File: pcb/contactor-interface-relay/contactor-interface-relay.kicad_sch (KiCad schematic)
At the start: 11 parts, among them J1 Conn_01x04_Socket, K1 G5LE-1

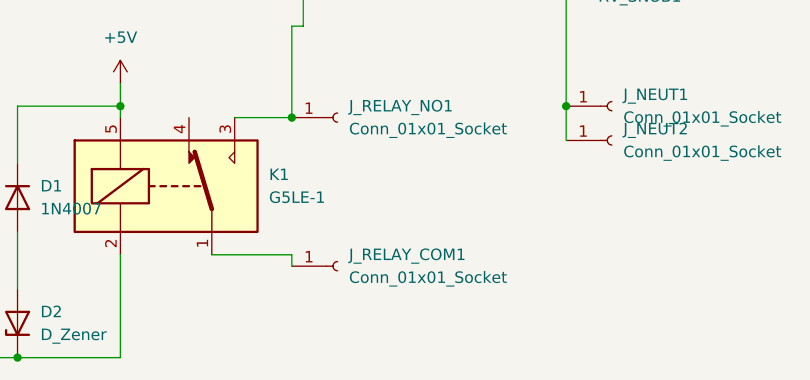
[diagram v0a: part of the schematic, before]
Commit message: Adding fuse for contactor coil
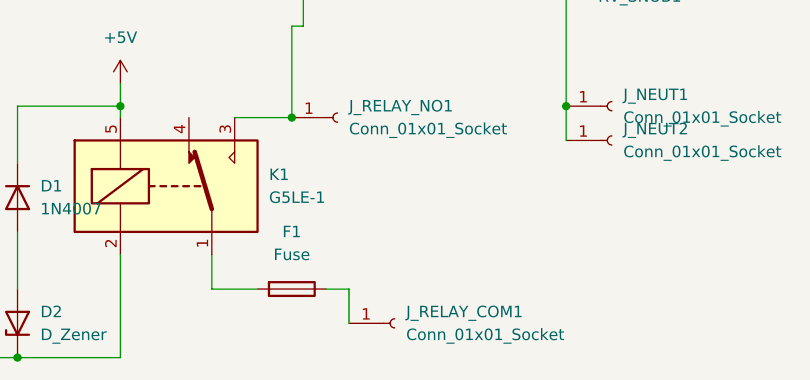
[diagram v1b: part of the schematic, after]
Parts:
- added F1: Fuse, Fuse:Fuse_Littelfuse_395Series, symbol Device:Fuse
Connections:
- net at J_RELAY_COM1.1 (Pin_1): now also F1.1; no longer K1.1
- new net: F1.2, K1.1
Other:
- moved on the sheet: J_RELAY_COM1
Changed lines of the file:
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@@
-	(wire
-		(pts
-			(xy 109.22 78.74) (xy 118.11 78.74)
-		)
-		(stroke
-			(width 0)
-			(type default)
-		)
-	)
 	(wire
 		(pts
@@
 	(wire
 		(pts
+			(xy 109.22 82.55) (xy 109.22 78.74)
+		)
+		(stroke
+			(width 0)
+			(type default)
+		)
+	)
+	(wire
+		(pts
 			(xy 99.06 62.23) (xy 99.06 63.5)
 		)
@@
 	(wire
 		(pts
+			(xy 121.92 82.55) (xy 124.46 82.55)
+		)
+		(stroke
+			(width 0)
+			(type default)
+		)
+	)
+	(wire
+		(pts
 			(xy 78.74 90.17) (xy 87.63 90.17)
 		)
@@
 	(wire
 		(pts
+			(xy 109.22 82.55) (xy 114.3 82.55)
+		)
+		(stroke
+			(width 0)
+			(type default)
+		)
+	)
+	(wire
+		(pts
 			(xy 111.76 63.5) (xy 118.11 63.5)
 		)
@@
 	(wire
 		(pts
-			(xy 118.11 78.74) (xy 118.11 80.01)
+			(xy 124.46 82.55) (xy 124.46 86.36)
 		)
 		(stroke
@@
 	)
 	(symbol
+		(lib_id "Device:Fuse")
+		(at 118.11 82.55 270)
+		(unit 1)
+		(exclude_from_sim no)
+		(in_bom yes)
+		(on_board yes)
+		(dnp no)
+		(fields_autoplaced yes)
+		(property "Reference" "F1"
+			(at 118.11 76.2 90)
+			(effects
+				(font
+					(size 1.27 1.27)
+				)
+			)
+		)
+		(property "Value" "Fuse"
+			(at 118.11 78.74 90)
+			(effects
+				(font
+					(size 1.27 1.27)
+				)
+			)
+		)
+		(property "Footprint" "Fuse:Fuse_Littelfuse_395Series"
+			(at 118.11 80.772 90)
+			(effects
+				(font
+					(size 1.27 1.27)
+				)
+				(hide yes)
+			)
+		)
+		(property "Datasheet" "~"
+			(at 118.11 82.55 0)
+			(effects
+				(font
+					(size 1.27 1.27)
+				)
+				(hide yes)
+			)
+		)
+		(property "Description" "Fuse"
+			(at 118.11 82.55 0)
+			(effects
+				(font
+					(size 1.27 1.27)
+				)
+				(hide yes)
+			)
+		)
+		(pin "1"
+		)
+		(pin "2"
+		)
+		(instances
+			(project ""
+				(path "/92cf2299-4756-44c6-9b64-4b60cc6635f5"
+					(reference "F1")
+					(unit 1)
+				)
+			)
+		)
+	)
+	(symbol
 		(lib_id "power:NEUT")
 		(at 124.46 48.26 0)
@@
 	(symbol
 		(lib_id "Connector:Conn_01x01_Socket")
-		(at 123.19 80.01 0)
+		(at 129.54 86.36 0)
 		(unit 1)
 		(exclude_from_sim no)
@@
 		(fields_autoplaced yes)
 		(property "Reference" "J_RELAY_COM1"
-			(at 124.46 78.7399 0)
+			(at 130.81 85.0899 0)
 			(effects
 				(font
@@
 		)
 		(property "Value" "Conn_01x01_Socket"
-			(at 124.46 81.2799 0)
+			(at 130.81 87.6299 0)
 			(effects
 				(font
@@
 		)
 		(property "Footprint" "Connector_Wire:SolderWire-2.5sqmm_1x01_D2.4mm_OD4.4mm"
-			(at 123.19 80.01 0)
+			(at 129.54 86.36 0)
 			(effects
 				(font
@@
 		)
 		(property "Datasheet" "~"
-			(at 123.19 80.01 0)
+			(at 129.54 86.36 0)
 			(effects
 				(font
@@
 		)
 		(property "Description" "Generic connector, single row, 01x01, script generated"
-			(at 123.19 80.01 0)
-			(effects
-				(font
+			(at 129.54 86.36 0)
+			(effects
+				(font

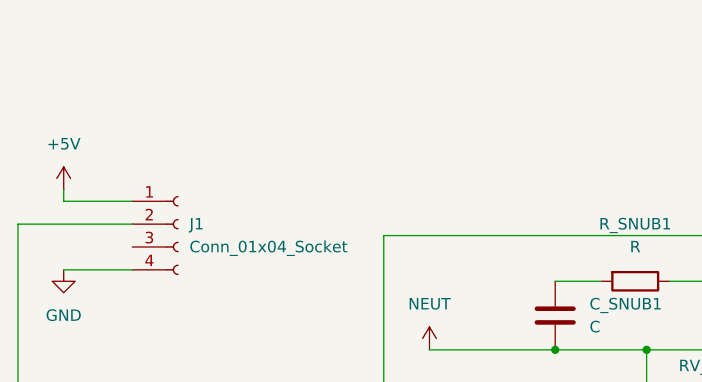
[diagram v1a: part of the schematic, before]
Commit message: Extra 5v / ground connections
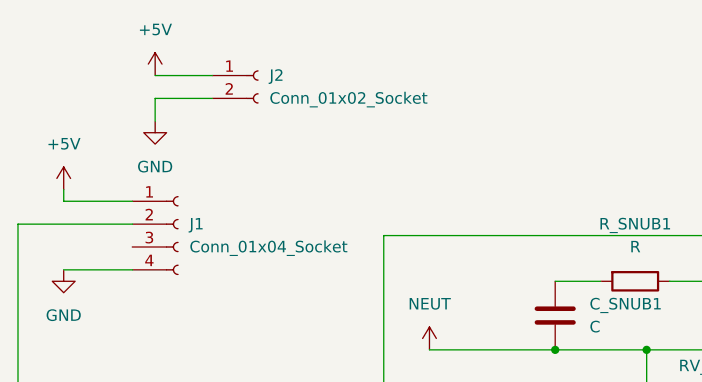
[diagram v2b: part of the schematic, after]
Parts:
- added J2: Conn_01x02_Socket, Connector_PinHeader_2.54mm:PinHeader_1x02_P2.54mm_Vertical, symbol Connector:Conn_01x02_Socket
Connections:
- net +5V: now also J2.1 (Pin_1)
- net GND: now also J2.2 (Pin_2)
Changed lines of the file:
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@@
+	(wire
+		(pts
+			(xy 93.98 17.78) (xy 100.33 17.78)
+		)
+		(stroke
+			(width 0)
+			(type default)
+		)
+	)
 	(wire
 		(pts
@@
 	(wire
 		(pts
+			(xy 93.98 20.32) (xy 93.98 22.86)
+		)
+		(stroke
+			(width 0)
+			(type default)
+		)
+	)
+	(wire
+		(pts
 			(xy 83.82 39.37) (xy 91.44 39.37)
 		)
@@
 	(wire
 		(pts
+			(xy 100.33 20.32) (xy 93.98 20.32)
+		)
+		(stroke
+			(width 0)
+			(type default)
+		)
+	)
+	(wire
+		(pts
 			(xy 91.44 31.75) (xy 83.82 31.75)
 		)
@@
 			(width 0)
 			(type default)
+		)
+	)
+	(symbol
+		(lib_id "Connector:Conn_01x02_Socket")
+		(at 105.41 17.78 0)
+		(unit 1)
+		(exclude_from_sim no)
+		(in_bom yes)
+		(on_board yes)
+		(dnp no)
+		(fields_autoplaced yes)
+		(property "Reference" "J2"
+			(at 106.68 17.7799 0)
+			(effects
+				(font
+					(size 1.27 1.27)
+				)
+				(justify left)
+			)
+		)
+		(property "Value" "Conn_01x02_Socket"
+			(at 106.68 20.3199 0)
+			(effects
+				(font
+					(size 1.27 1.27)
+				)
+				(justify left)
+			)
+		)
+		(property "Footprint" "Connector_PinHeader_2.54mm:PinHeader_1x02_P2.54mm_Vertical"
+			(at 105.41 17.78 0)
+			(effects
+				(font
+					(size 1.27 1.27)
+				)
+				(hide yes)
+			)
+		)
+		(property "Datasheet" "~"
+			(at 105.41 17.78 0)
+			(effects
+				(font
+					(size 1.27 1.27)
+				)
+				(hide yes)
+			)
+		)
+		(property "Description" "Generic connector, single row, 01x02, script generated"
+			(at 105.41 17.78 0)
+			(effects
+				(font
+					(size 1.27 1.27)
+				)
+				(hide yes)
+			)
+		)
+		(pin "1"
+		)
+		(pin "2"
+		)
+		(instances
+			(project ""
+				(path "/92cf2299-4756-44c6-9b64-4b60cc6635f5"
+					(reference "J2")
+					(unit 1)
+				)
+			)
 		)
 	)
@@
 	)
 	(symbol
+		(lib_id "power:GND")
+		(at 93.98 22.86 0)
+		(unit 1)
+		(exclude_from_sim no)
+		(in_bom yes)
+		(on_board yes)
+		(dnp no)
+		(fields_autoplaced yes)
+		(property "Reference" "#PWR6"
+			(at 93.98 29.21 0)
+			(effects
+				(font
+					(size 1.27 1.27)
+				)
+				(hide yes)
+			)
+		)
+		(property "Value" "GND"
+			(at 93.98 27.94 0)
+			(effects
+				(font
+					(size 1.27 1.27)
+				)
+			)
+		)
+		(property "Footprint" ""
+			(at 93.98 22.86 0)
+			(effects
+				(font
+					(size 1.27 1.27)
+				)
+				(hide yes)
+			)
+		)
+		(property "Datasheet" ""
+			(at 93.98 22.86 0)
+			(effects
+				(font
+					(size 1.27 1.27)
+				)
+				(hide yes)
+			)
+		)
+		(property "Description" "Power symbol creates a global label with name \"GND\" , ground"
+			(at 93.98 22.86 0)
+			(effects
+				(font
+					(size 1.27 1.27)
+				)
+				(hide yes)
+			)
+		)
+		(pin "1"
+		)
+		(instances
+			(project ""
+				(path "/92cf2299-4756-44c6-9b64-4b60cc6635f5"
+					(reference "#PWR6")
+					(unit 1)
+				)
+			)
+		)
+	)
+	(symbol
 		(lib_id "Connector:Conn_01x01_Socket")
 		(at 129.54 86.36 0)
@@
 					(unit 1)
 				)
+			)
+		)
+	)
+	(symbol
+		(lib_id "power:+5V")
+		(at 93.98 17.78 0)
+		(unit 1)
+		(exclude_from_sim no)
+		(in_bom yes)
+		(on_board yes)
+		(dnp no)
+		(fields_autoplaced yes)
+		(property "Reference" "#PWR5"
+			(at 93.98 21.59 0)
+			(effects
+				(font
+					(size 1.27 1.27)
+				)
+				(hide yes)
+			)
+		)
+		(property "Value" "+5V"
+			(at 93.98 12.7 0)
+			(effects
+				(font
+					(size 1.27 1.27)
+				)
+			)
+		)
+		(property "Footprint" ""
+			(at 93.98 17.78 0)
+			(effects
+				(font
+					(size 1.27 1.27)
+				)
+				(hide yes)
+			)
+		)
+		(property "Datasheet" ""
+			(at 93.98 17.78 0)
+			(effects
+				(font
+					(size 1.27 1.27)
+				)
+				(hide yes)
+			)
+		)
+		(property "Description" "Power symbol creates a global label with name \"+5V\""
+			(at 93.98 17.78 0)
+			(effects
+				(font
+					(size 1.27 1.27)
+				)
+				(hide yes)
+			)
+		)
+		(pin "1"
+		)
+		(instances
+			(project ""
+				(path "/92cf2299-4756-44c6-9b64-4b60cc6635f5"
+					(reference "#PWR5")
+					(unit 1)
+				)
